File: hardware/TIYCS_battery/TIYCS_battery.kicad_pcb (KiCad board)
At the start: 2 copper layers, 100 x 100 mm, 23 parts, among them J1 Barrel_Jack_Switch, J2 External Jack, J3 pinHeaders, U1 4S_BMS, U2 4_18650, U3 XL4015

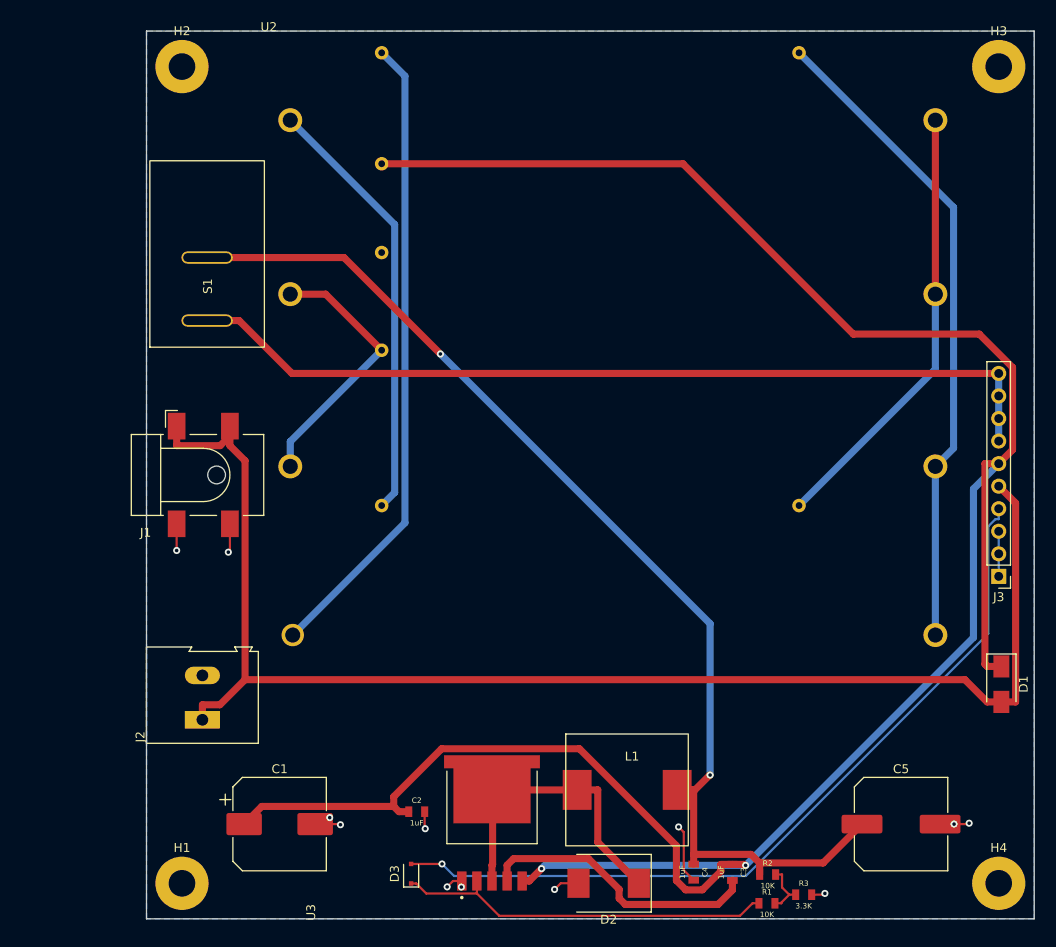
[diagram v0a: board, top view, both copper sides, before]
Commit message: Moved switch, cleared PCB file, changed voltage divider
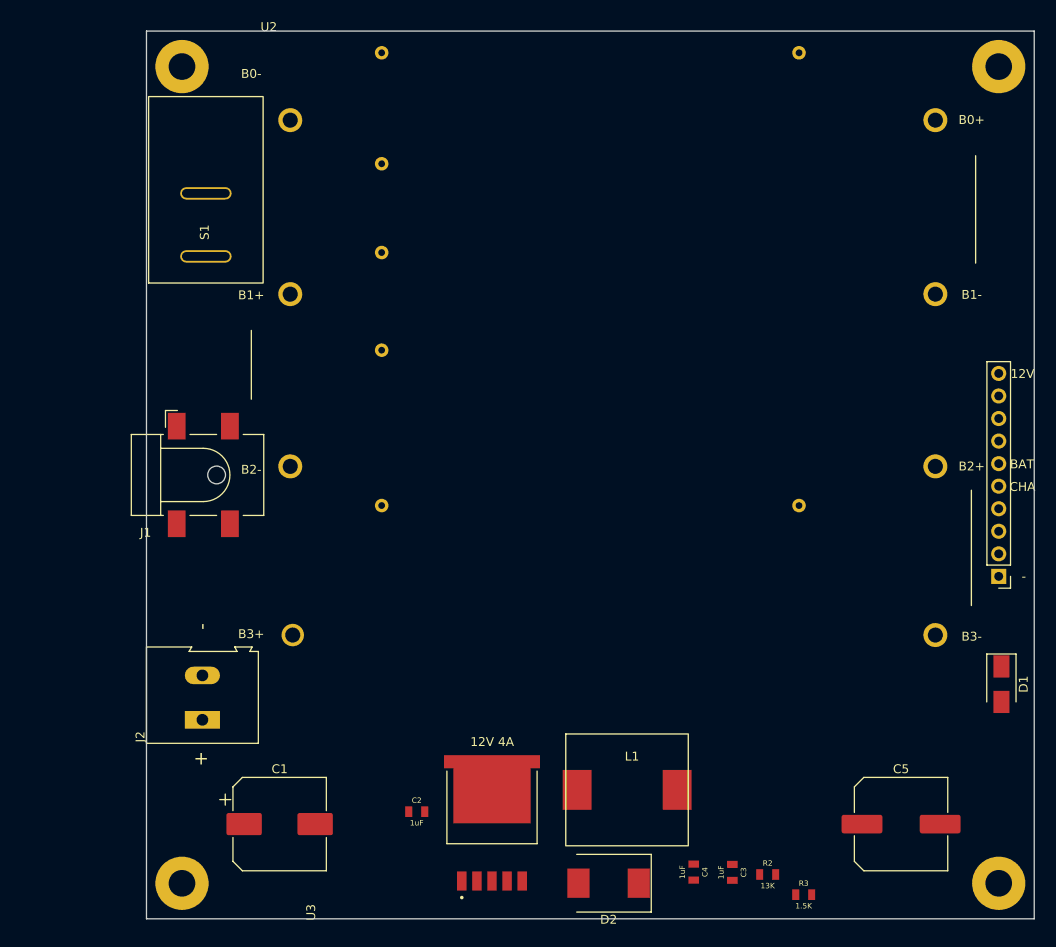
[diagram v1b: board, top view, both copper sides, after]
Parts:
- removed D3: 1N4148, Diode_SMD:D_SOD-323F
- removed R1: 10K, Resistors:0805
- R2: value 10K -> 13K
- R3: value 3.3K -> 1.5K
- moved S1 7.23 mm to (6.69, 25.4)
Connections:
- C4 pad 1: Net-(C4-Pad1) -> +12V
- C5 pad 1: Net-(C4-Pad1) -> +12V
- J3 pad 4: EN -> GND
- L1 pad 2: Net-(C4-Pad1) -> +12V
- R2 pad 1: Net-(C4-Pad1) -> +12V
- R2 pad 2: Net-(R1-Pad2) -> Net-(U3-Pad2)
- R3 pad 1: Net-(R1-Pad2) -> Net-(U3-Pad2)
- S1 pad 1: +12V -> Net-(U1-Pad6)
- S1 pad 2: Net-(C4-Pad1) -> V_SENSE_BAT
- U1 pad 6: V_SENSE_BAT -> Net-(U1-Pad6)
- U3 pad 2: Net-(D3-Pad1) -> Net-(U3-Pad2)
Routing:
- net V_SENSE_BAT: track 274.3 -> 0.00 mm, vias 2 -> 0
- net V_SENSE: track 158.5 -> 0.00 mm
- net Net-(C4-Pad1): track 126.0 -> 0.00 mm, vias 2 -> 0
- net +12V: track 99.3 -> 0.00 mm
- net EN: track 91.7 -> 0.00 mm, vias 1 -> 0
- net Net-(U1-Pad4): track 73.6 -> 0.00 mm
- net Net-(U1-Pad5): track 71.9 -> 0.00 mm
- net Net-(U1-Pad2): track 49.8 -> 0.00 mm
- net Net-(U1-Pad1): track 48.9 -> 0.00 mm
- net Net-(D3-Pad1): track 42.7 -> 0.00 mm
- net Net-(D2-Pad1): track 34.7 -> 0.00 mm
- net GND: track 33.4 -> 0.00 mm, vias 12 -> 0
- net Net-(C3-Pad2): track 32.0 -> 0.00 mm
- net Net-(U1-Pad3): track 30.3 -> 0.00 mm
- net Net-(R1-Pad2): track 6.12 -> 0.00 mm
- removed copper zone on B.Cu, net GND
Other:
- board text added: "+"
- board text added: "-"
- board text added: "12V"
- board text added: "12V 4A"
- board text added: "B0+"
- board text added: "B0-"
- board text added: "B1+"
- board text added: "B1-"
- board text added: "B2+"
- board text added: "B2-"
- board text added: "B3+"
- board text added: "B3-"
- board text added: "BAT"
- board text added: "CHA"

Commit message: Start with new LDO, fuse
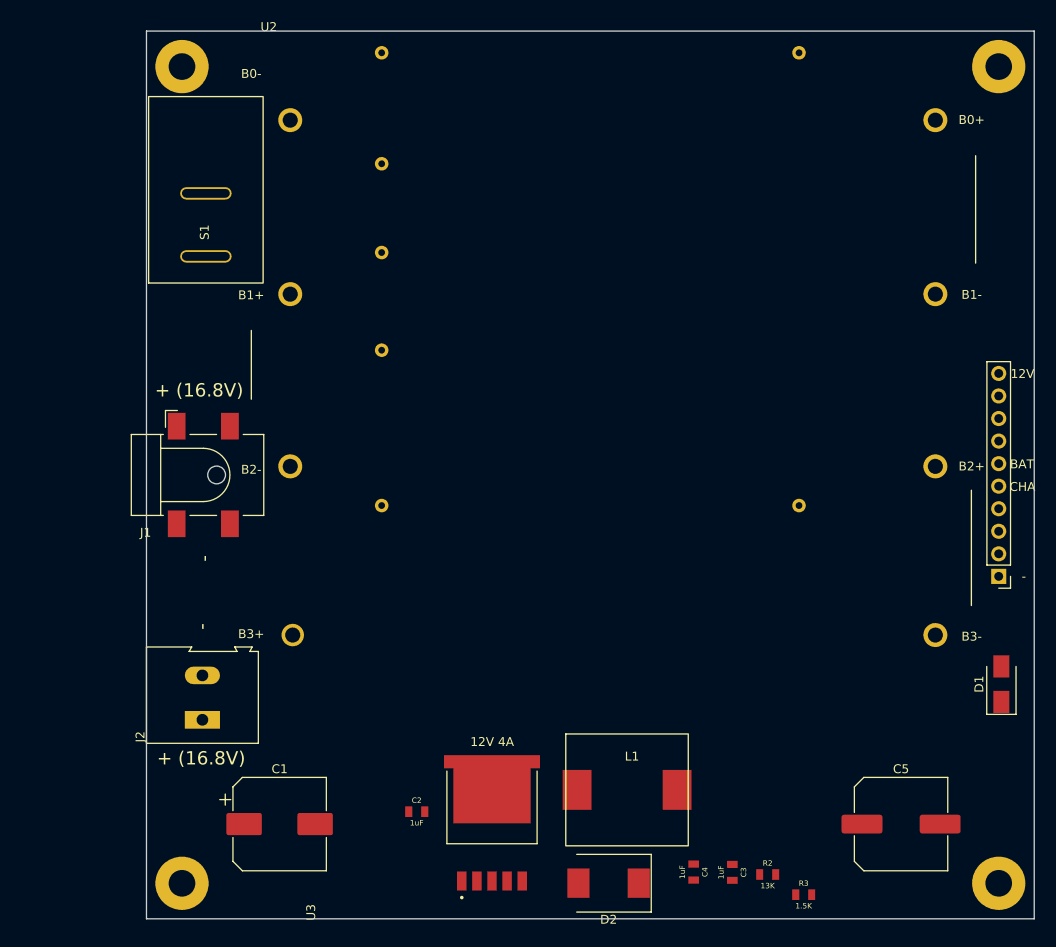
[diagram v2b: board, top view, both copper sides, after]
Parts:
- turned D1 to 90 degrees
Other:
- board text added: "+ (16.8V)"
- board text removed: "+"
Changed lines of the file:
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@@
   )
   (footprint "Diode_SMD:D_SMA" (layer "F.Cu")
-    (at 96.3 73.57 -90)
+    (at 96.3 73.57 90)
     (descr "Diode SMA (DO-214AC)")
     (tags "Diode SMA (DO-214AC)")
@@
     (property "Sheetname" "")
     (attr smd)
-    (fp_text reference "D1" (at 0 -2.5 -270) (layer "F.SilkS")
-      (effects (font (size 1 1) (thickness 0.15)))
-    )
-    (fp_text value "D" (at 0 2.6 -270) (layer "F.Fab")
-      (effects (font (size 1 1) (thickness 0.15)))
-    )
-    (fp_text user "${REFERENCE}" (at 0 -2.5 -270) (layer "F.Fab")
+    (fp_text reference "D1" (at 0 -2.5 90) (layer "F.SilkS")
+      (effects (font (size 1 1) (thickness 0.15)))
+    )
+    (fp_text value "D" (at 0 2.6 90) (layer "F.Fab")
+      (effects (font (size 1 1) (thickness 0.15)))
+    )
+    (fp_text user "${REFERENCE}" (at 0 -2.5 90) (layer "F.Fab")
       (effects (font (size 1 1) (thickness 0.15)))
     )
@@
     (fp_line (start 0.50118 0.00102) (end 1.4994 0.00102) (layer "F.Fab") (width 0.1))
     (fp_line (start -0.64944 0.00102) (end 0.50118 -0.79908) (layer "F.Fab") (width 0.1))
-    (pad "1" smd rect locked (at -2 0 270) (size 2.5 1.8) (layers "F.Cu" "F.Paste" "F.Mask")
+    (pad "1" smd rect locked (at -2 0 90) (size 2.5 1.8) (layers "F.Cu" "F.Paste" "F.Mask")
       (net 1 "V_SENSE_BAT") (pinfunction "K") (pintype "passive"))
-    (pad "2" smd rect locked (at 2 0 270) (size 2.5 1.8) (layers "F.Cu" "F.Paste" "F.Mask")
+    (pad "2" smd rect locked (at 2 0 90) (size 2.5 1.8) (layers "F.Cu" "F.Paste" "F.Mask")
       (net 5 "V_SENSE") (pinfunction "A") (pintype "passive"))
     (model "${KICAD6_3DMODEL_DIR}/Diode_SMD.3dshapes/D_SMA.wrl"
@@
     (effects (font (size 1.5 1.5) (thickness 0.3)))
   )
+  (gr_text "+ (16.8V)" (at 5.93 40.47) (layer "F.SilkS")
+    (effects (font (size 1.5 1.5) (thickness 0.3)))
+  )
   (gr_text "CHA" (at 98.67 51.34) (layer "F.SilkS")
     (effects (font (size 1 1) (thickness 0.15)))
   )
-  (gr_text "+" (at 6.16 81.92) (layer "F.SilkS")
+  (gr_text "+ (16.8V)" (at 6.16 81.92) (layer "F.SilkS")
     (effects (font (size 1.5 1.5) (thickness 0.3)))
   )
@@
     (effects (font (size 1 1) (thickness 0.15)))
   )
+  (gr_text "-" (at 6.49 59.4 90) (layer "F.SilkS")
+    (effects (font (size 1.5 1.5) (thickness 0.3)))
+  )
   (gr_text "BAT" (at 98.62 48.79) (layer "F.SilkS")

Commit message: First version of ledPanel: board outline + pins
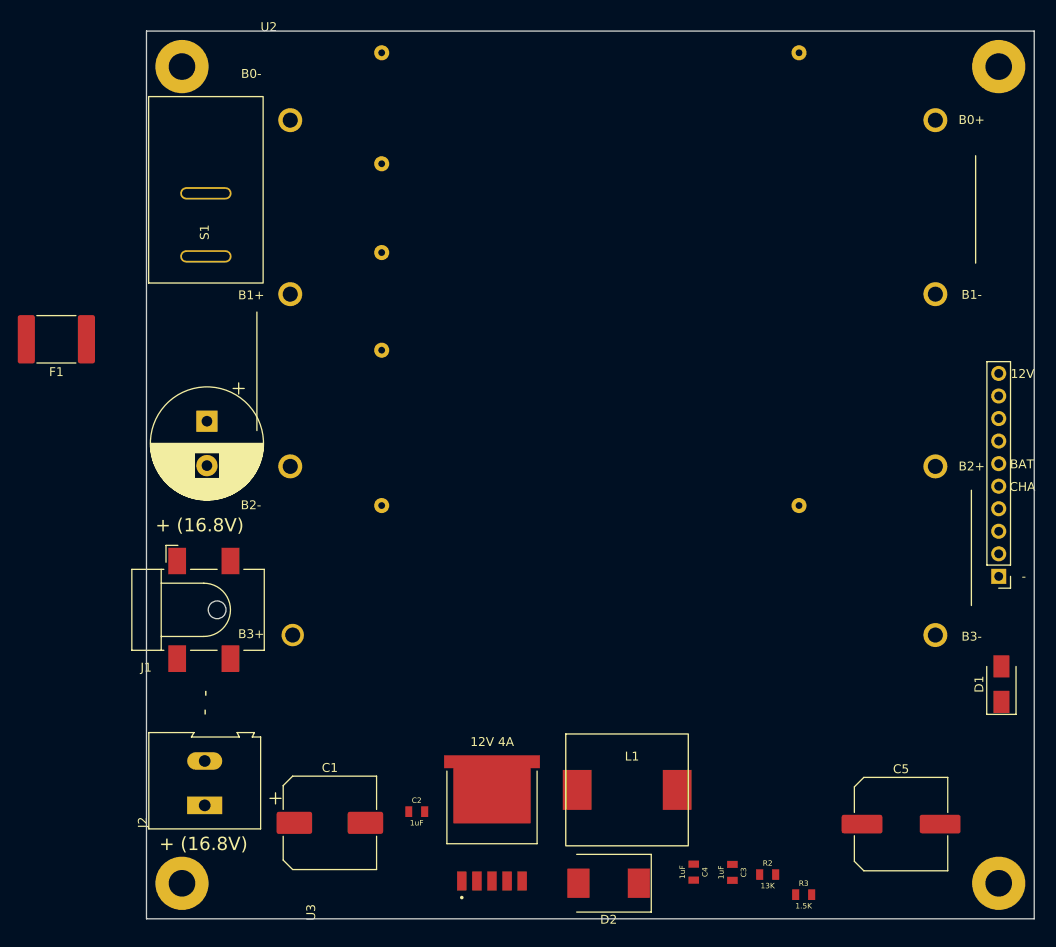
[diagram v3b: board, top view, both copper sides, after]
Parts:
- added C6: C_Polarized, Capacitor_THT:CP_Radial_D12.5mm_P5.00mm, F.Cu at (6.81, 44.0)
- added F1: Fuse, Fuse:Fuse_2920_7451Metric, F.Cu at (-10.2, 34.7)
- moved J1 15.2 mm to (6.46, 65.2)
- moved J2 9.64 mm to (6.56, 87.2)
- moved C1 5.66 mm to (20.7, 89.2)

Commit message: Routed battery PCB
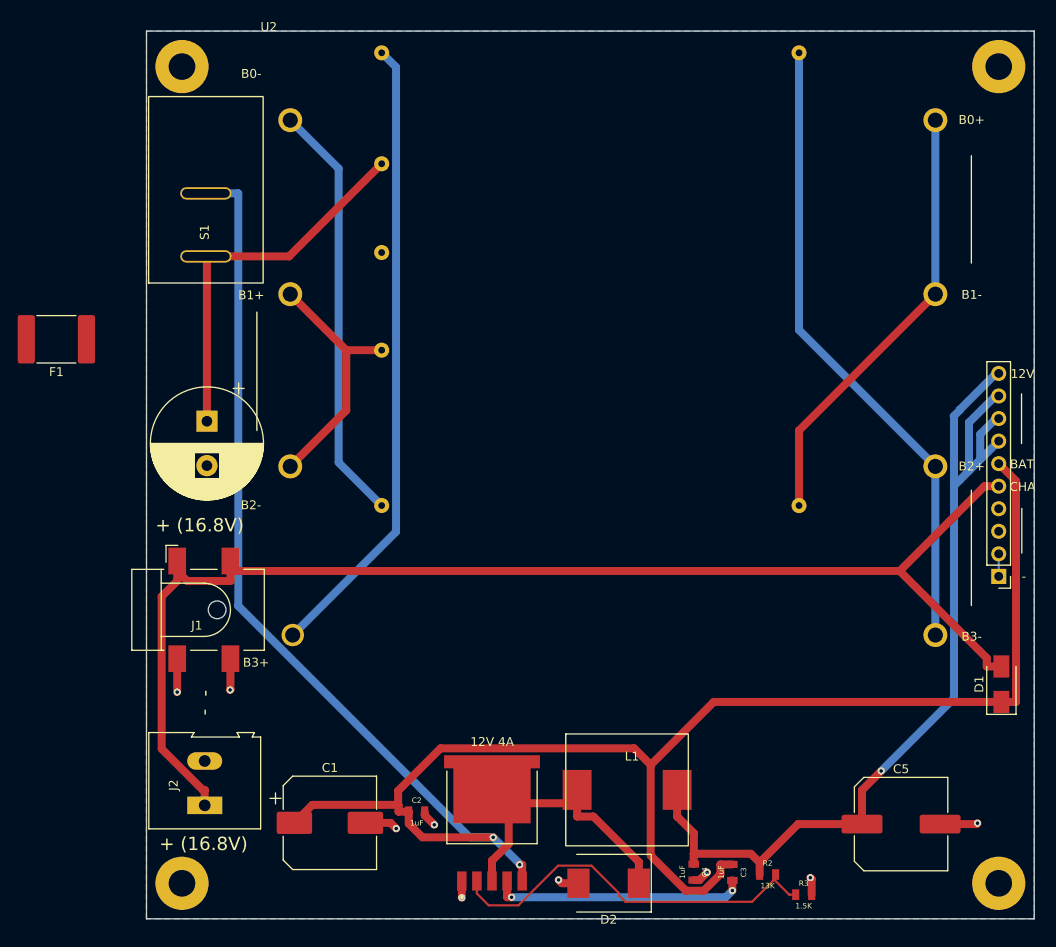
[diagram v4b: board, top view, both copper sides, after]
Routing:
- net V_SENSE_BAT: track 0.00 -> 249.5 mm, vias 0 -> 2
- net V_SENSE: track 0.00 -> 146.1 mm
- net +12V: track 0.00 -> 111.9 mm, vias 0 -> 1
- net Net-(U1-Pad4): track 0.00 -> 71.9 mm
- net Net-(U1-Pad5): track 0.00 -> 71.1 mm
- net Net-(U1-Pad2): track 0.00 -> 49.8 mm
- net Net-(U1-Pad1): track 0.00 -> 47.7 mm
- net Net-(R2-Pad2): track 0.00 -> 43.9 mm
- net Net-(C6-Pad1): track 0.00 -> 42.7 mm
- net Net-(D2-Pad1): track 0.00 -> 34.3 mm
- net Net-(C3-Pad2): track 0.00 -> 28.7 mm, vias 0 -> 2
- net Net-(U1-Pad3): track 0.00 -> 28.6 mm
- net GND: track 0.00 -> 28.2 mm, vias 0 -> 9
- added copper zone on B.Cu, net GND
